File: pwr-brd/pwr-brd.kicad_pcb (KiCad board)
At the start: 2 copper layers, 30 parts, among them J1 PWRIN, J2 CTRLIN, J3 PWROUT, J4 PWROUT, J5 PWROUT, J6 PWROUT, U1 TPS27SA08CPWPR, U2 TPS27SA08CPWPR

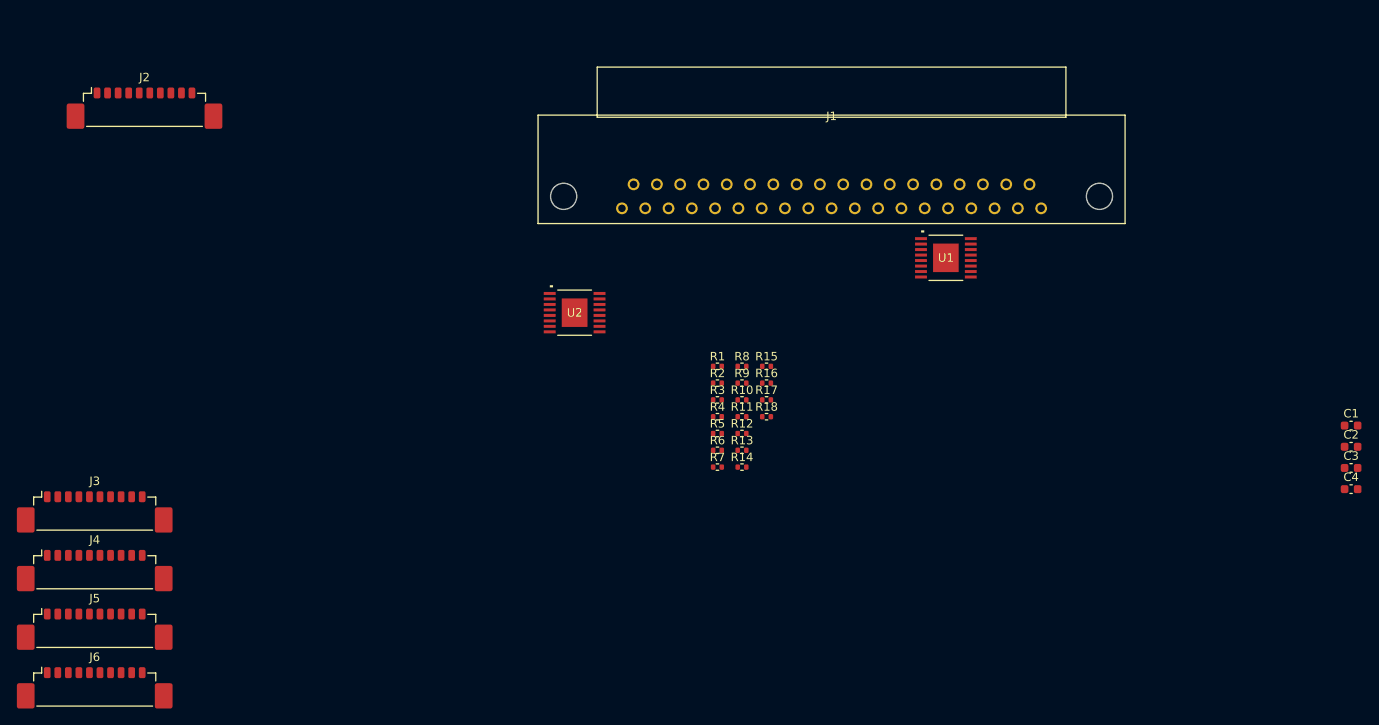
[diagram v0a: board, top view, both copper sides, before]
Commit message: Laid out inrush limiter
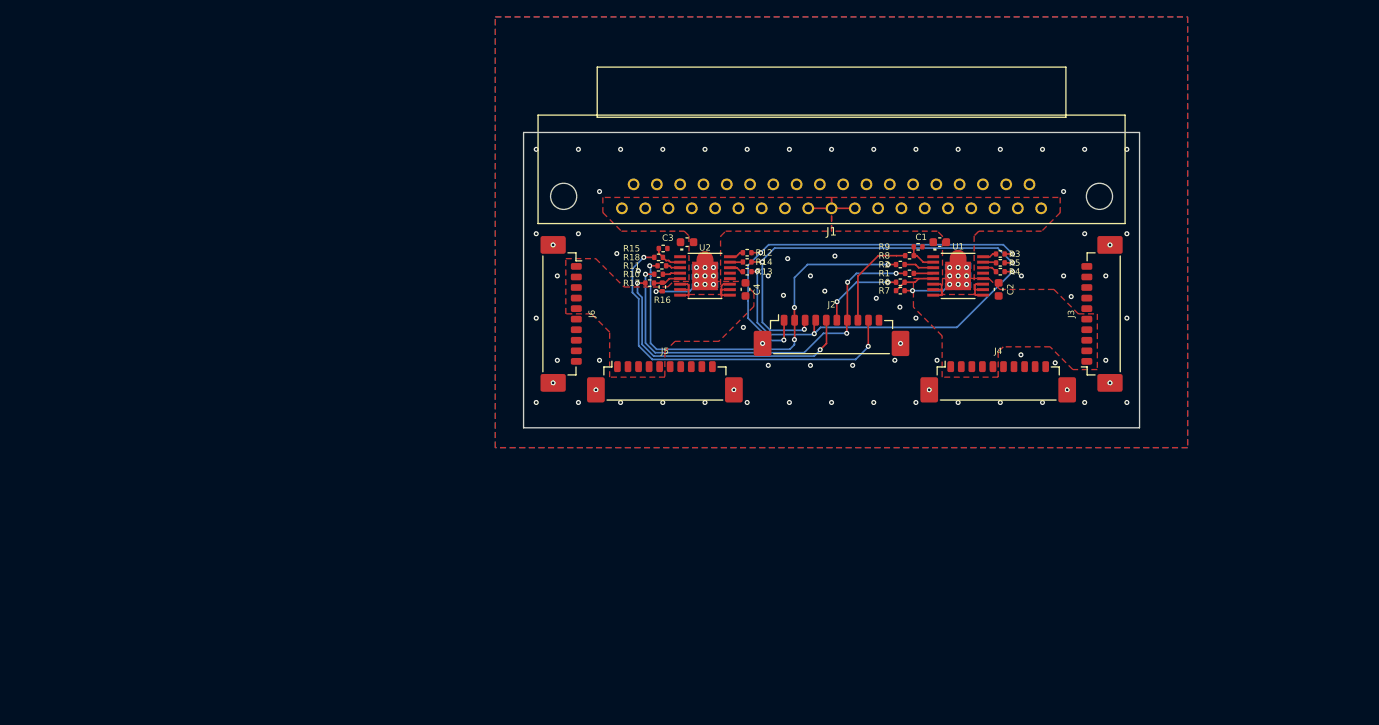
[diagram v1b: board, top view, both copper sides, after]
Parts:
- moved J3 121.0 mm to (153.4, 77.2), turned to 90 degrees
- moved J4 109.4 mm to (141.7, 84.7)
- moved J2 85.8 mm to (122.0, 79.2)
- moved C3 83.1 mm to (104.8, 68.7)
- moved C4 75.6 mm to (111.8, 74.3), turned to 90 degrees
- moved J5 73.7 mm to (102.2, 84.7)
- moved J6 70.9 mm to (90.5, 77.2), turned to -90 degrees
- moved C1 53.4 mm to (134.8, 68.7)
- moved C2 45.7 mm to (141.8, 74.3), turned to 90 degrees
- moved R5 39.2 mm to (141.9, 71.2), turned to 180 degrees
- moved R3 37.7 mm to (141.9, 70.1), turned to 180 degrees
- moved R4 37.7 mm to (141.9, 72.2), turned to 180 degrees
- moved R7 30.1 mm to (130.1, 74.5), turned to 180 degrees
- moved R6 29.4 mm to (130.1, 73.5)
- moved R9 26.4 mm to (132.2, 69.3)
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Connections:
- J1 pad 19: unconnected-(J1-Pin_19-Pad19) -> Vdrive
- U1 pad EP: (no net) -> Vdrive
- U2 pad EP: (no net) -> Vdrive
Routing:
- net /DEN: track 0.00 -> 48.8 mm, vias 0 -> 3
- net /LATCH: track 0.00 -> 48.4 mm, vias 0 -> 4
- net /EN: track 0.00 -> 47.8 mm, vias 0 -> 4
- net /SEL2: track 0.00 -> 47.1 mm, vias 0 -> 3
- net /SNS_2: track 0.00 -> 44.2 mm, vias 0 -> 2
- net /SEL1: track 0.00 -> 43.3 mm, vias 0 -> 3
- net /ST_2: track 0.00 -> 34.3 mm, vias 0 -> 2
- net Vdrive: track 0.00 -> 21.1 mm, vias 0 -> 20
- net /SNS_1: track 0.00 -> 11.8 mm
- net /ST_1: track 0.00 -> 10.2 mm, vias 0 -> 2
- net V_{B}: track 0.00 -> 8.95 mm
- net V_{A}: track 0.00 -> 8.35 mm
- net /ST_1_IN: track 0.00 -> 5.00 mm
- net /SNS_1_IN: track 0.00 -> 3.67 mm
- net /LT_1: track 0.00 -> 3.55 mm
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- added copper zone on B.Cu, net GND
- added copper zone on F.Cu, net GND
- added copper zone on F.Cu, net V_{A}
- added copper zone on F.Cu, net V_{B}
- added copper zone on B.Cu, net Vdrive
- added copper zone on F.Cu, net Vdrive
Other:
- board outline added: 73 x 35 mm
